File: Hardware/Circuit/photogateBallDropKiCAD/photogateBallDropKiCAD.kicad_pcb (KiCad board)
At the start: 2 copper layers, 127 x 68.6 mm, 56 parts, among them Q1 2N3906, Q2 2N3904, Q3 2N3904, Q4 BPW40, Q5 2N3904, Q6 2N3904, Q7 2N3904, Q8 2N3904, SW2 SW_SPDT, U2 LM358

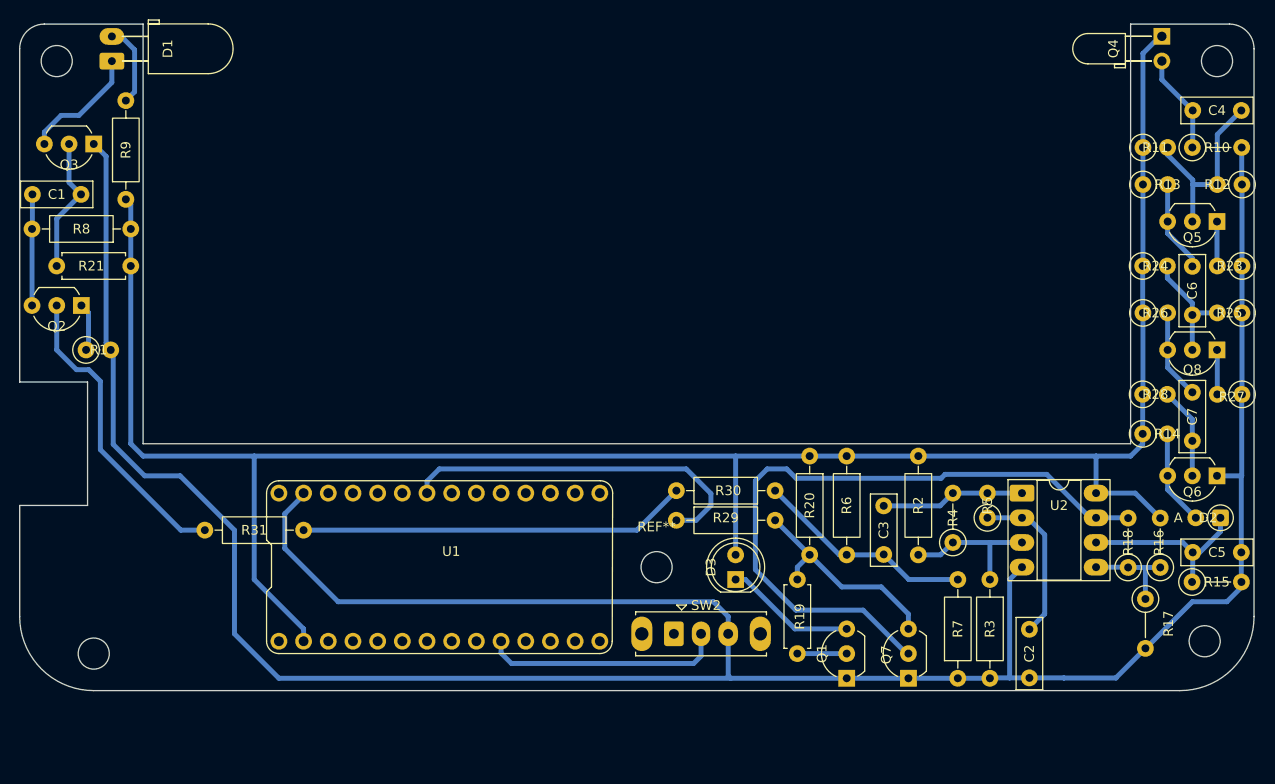
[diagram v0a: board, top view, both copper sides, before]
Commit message: Add photogate PCB
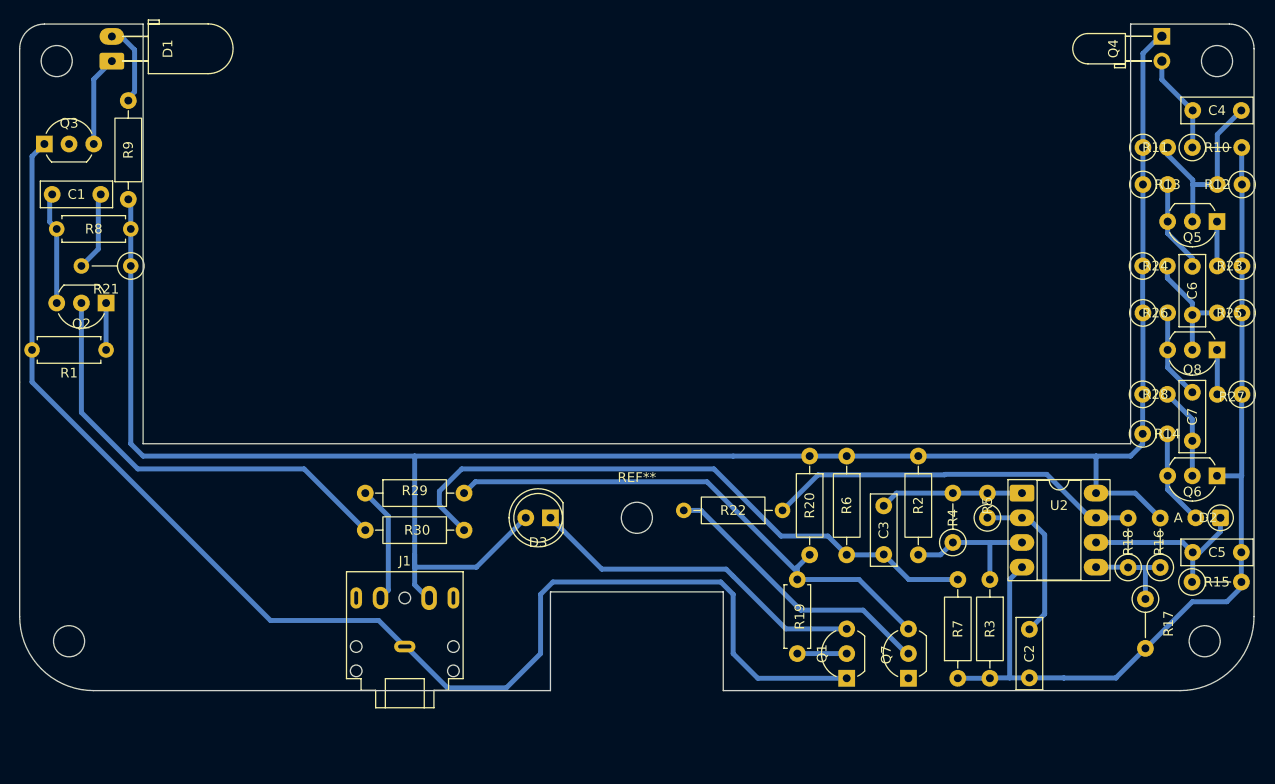
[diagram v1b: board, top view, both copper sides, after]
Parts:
- removed R31: 0, Resistor_THT:R_Axial_DIN0207_L6.3mm_D2.5mm_P10.16mm_Horizontal
- removed SW2: SW_SPDT, User:SlideSwitch_SPDT
- removed U1: ~, User:AdafruitItsyBitsyM0
- added J1: AudioJack3_SwitchTR, Connector_Audio:Jack_3.5mm_CUI_SJ1-3525N_Horizontal, F.Cu at (65.0, 89.4)
- added R22: 0, Resistor_THT:R_Axial_DIN0207_L6.3mm_D2.5mm_P10.16mm_Horizontal, F.Cu at (103.9, 75.4)
- C4: value 4n7 -> 1n
- R1: footprint Resistor_THT:R_Axial_DIN0207_L6.3mm_D2.5mm_P2.54mm_Vertical -> Resistor_THT:R_Axial_DIN0207_L6.3mm_D2.5mm_P7.62mm_Horizontal
- R21: footprint Resistor_THT:R_Axial_DIN0207_L6.3mm_D2.5mm_P7.62mm_Horizontal -> Resistor_THT:R_Axial_DIN0207_L6.3mm_D2.5mm_P5.08mm_Vertical
- R8: footprint Resistor_THT:R_Axial_DIN0207_L6.3mm_D2.5mm_P10.16mm_Horizontal -> Resistor_THT:R_Axial_DIN0207_L6.3mm_D2.5mm_P7.62mm_Horizontal
- moved R30 32.3 mm to (71.1, 77.5)
- moved R29 32.1 mm to (61.0, 73.7)
- moved D3 20.1 mm to (80.0, 76.2), turned to 180 degrees
- moved REF** 5.47 mm to (88.9, 76.2)
- moved Q3 5.08 mm to (27.9, 37.7), turned to 0 degrees
- moved REF** 2.84 mm to (30.5, 88.9)
- moved Q2 2.55 mm to (34.3, 54.1)
- moved R1 2.06 mm to (34.3, 58.9), turned to 180 degrees
- moved C1 2.03 mm to (28.7, 42.9)
- moved R9 0.25 mm to (36.6, 43.4)
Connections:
- R18 pad 2: Net-(Q7-B) -> Net-(R18-Pad2)
- R30 pad 2: Net-(R30-Pad2) -> Net-(Q2-B)
- U2 pad 7: Net-(Q7-B) -> Net-(R18-Pad2)
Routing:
- net GND: track 289.1 -> 230.5 mm
- net Net-(C3-Pad2): track 22.6 -> 64.1 mm
- net Net-(Q7-B): track 69.8 -> 29.2 mm
- net Net-(R30-Pad2): track 40.0 -> 0.00 mm
- net Net-(R18-Pad2): track 0.00 -> 39.0 mm
- net Net-(Q7-C): track 22.3 -> 56.0 mm
- net INT: track 37.4 -> 12.1 mm
- net Net-(SW2-B): track 24.8 -> 0.00 mm
- net Net-(D3-K): track 13.5 -> 35.2 mm
- net Net-(Q2-B): track 31.6 -> 45.5 mm
- net Net-(Q3-B): track 14.6 -> 8.09 mm
- net Net-(D1-K): track 12.5 -> 9.30 mm
- net VCC: track 216.2 -> 214.7 mm
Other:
- outline, holes or cut-outs redrawn

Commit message: edit PCB
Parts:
- J1: footprint Connector_Audio:Jack_3.5mm_CUI_SJ1-3525N_Horizontal -> Connector_Audio:Jack_3.5mm_CUI_SJ1-3523N_Horizontal
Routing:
- net GND: track 230.5 -> 241.9 mm
- net Net-(Q3-B): track 8.09 -> 14.6 mm
- net VCC: track 214.7 -> 212.6 mm
- net INT: track 12.1 -> 13.1 mm
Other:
- outline, holes or cut-outs redrawn
- board text removed: "SPDT Switch"

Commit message: edit photogate pcb
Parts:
- removed C7: 1n, Capacitor_THT:C_Rect_L7.2mm_W2.5mm_P5.00mm_FKS2_FKP2_MKS2_MKP2
- removed Q6: 2N3904, Package_TO_SOT_THT:TO-92_Inline_Wide
- removed R12, R14: 10k, Resistor_THT:R_Axial_DIN0207_L6.3mm_D2.5mm_P2.54mm_Vertical
- removed R21: 100k, Resistor_THT:R_Axial_DIN0207_L6.3mm_D2.5mm_P5.08mm_Vertical
- removed R22, R29, R30: 0, Resistor_THT:R_Axial_DIN0207_L6.3mm_D2.5mm_P10.16mm_Horizontal
- removed R23: 220, Resistor_THT:R_Axial_DIN0207_L6.3mm_D2.5mm_P2.54mm_Vertical
- removed R25: 100k, Resistor_THT:R_Axial_DIN0207_L6.3mm_D2.5mm_P2.54mm_Vertical
- removed R27: 1k, Resistor_THT:R_Axial_DIN0207_L6.3mm_D2.5mm_P2.54mm_Vertical
- removed R28: 1M, Resistor_THT:R_Axial_DIN0207_L6.3mm_D2.5mm_P2.54mm_Vertical
- added C10: 100u, Capacitor_THT:C_Radial_D8.0mm_H7.0mm_P3.50mm, F.Cu at (77.6, 81.0)
- added C11: 1u, Capacitor_THT:C_Rect_L7.2mm_W2.5mm_P5.00mm_FKS2_FKP2_MKS2_MKP2, F.Cu at (120.9, 77.5)
- added C12: 10u, Capacitor_THT:C_Rect_L7.2mm_W2.5mm_P5.00mm_FKS2_FKP2_MKS2_MKP2, F.Cu at (74.5, 91.9)
- added C9: 10u, Capacitor_THT:C_Rect_L7.2mm_W2.5mm_P5.00mm_FKS2_FKP2_MKS2_MKP2, F.Cu at (120.9, 73.8)
- C1: value 1n -> 10n
- C3: value 10n -> 1n
- C5: value 4n7 -> 1n
- D2: footprint Diode_THT:D_DO-35_SOD27_P2.54mm_Vertical_AnodeUp -> Diode_THT:D_DO-35_SOD27_P7.62mm_Horizontal
- J1: value AudioJack3_SwitchTR -> AudioJack3
- R1: value 2k2 -> 1k; footprint Resistor_THT:R_Axial_DIN0207_L6.3mm_D2.5mm_P7.62mm_Horizontal -> Resistor_THT:R_Axial_DIN0207_L6.3mm_D2.5mm_P10.16mm_Horizontal
- R10: value 360 -> 220; footprint Resistor_THT:R_Axial_DIN0207_L6.3mm_D2.5mm_P5.08mm_Vertical -> Resistor_THT:R_Axial_DIN0207_L6.3mm_D2.5mm_P7.62mm_Horizontal
- R11: value 22k -> 100k; footprint Resistor_THT:R_Axial_DIN0207_L6.3mm_D2.5mm_P2.54mm_Vertical -> Resistor_THT:R_Axial_DIN0207_L6.3mm_D2.5mm_P7.62mm_Horizontal
- R13: value 2k2 -> 10k; footprint Resistor_THT:R_Axial_DIN0207_L6.3mm_D2.5mm_P2.54mm_Vertical -> Resistor_THT:R_Axial_DIN0207_L6.3mm_D2.5mm_P7.62mm_Horizontal
- R15, R17, R4: footprint Resistor_THT:R_Axial_DIN0207_L6.3mm_D2.5mm_P5.08mm_Vertical -> Resistor_THT:R_Axial_DIN0207_L6.3mm_D2.5mm_P10.16mm_Horizontal
- R16: value 47k -> 100k; footprint Resistor_THT:R_Axial_DIN0207_L6.3mm_D2.5mm_P5.08mm_Vertical -> Resistor_THT:R_Axial_DIN0207_L6.3mm_D2.5mm_P10.16mm_Horizontal
- R18: value 33k -> 100k; footprint Resistor_THT:R_Axial_DIN0207_L6.3mm_D2.5mm_P5.08mm_Vertical -> Resistor_THT:R_Axial_DIN0207_L6.3mm_D2.5mm_P10.16mm_Horizontal
- R19: value 220 -> 1k; footprint Resistor_THT:R_Axial_DIN0207_L6.3mm_D2.5mm_P7.62mm_Horizontal -> Resistor_THT:R_Axial_DIN0207_L6.3mm_D2.5mm_P10.16mm_Horizontal
- R24: value 220k -> 1M; footprint Resistor_THT:R_Axial_DIN0207_L6.3mm_D2.5mm_P2.54mm_Vertical -> Resistor_THT:R_Axial_DIN0207_L6.3mm_D2.5mm_P7.62mm_Horizontal
- R26: footprint Resistor_THT:R_Axial_DIN0207_L6.3mm_D2.5mm_P2.54mm_Vertical -> Resistor_THT:R_Axial_DIN0207_L6.3mm_D2.5mm_P7.62mm_Horizontal
- R3: footprint Resistor_THT:R_Axial_DIN0207_L6.3mm_D2.5mm_P10.16mm_Horizontal -> Resistor_THT:R_Axial_DIN0207_L6.3mm_D2.5mm_P7.62mm_Horizontal
- R5: value 1k3 -> 1k; footprint Resistor_THT:R_Axial_DIN0207_L6.3mm_D2.5mm_P2.54mm_Vertical -> Resistor_THT:R_Axial_DIN0207_L6.3mm_D2.5mm_P7.62mm_Horizontal
- R6: value 22k -> 1M; footprint Resistor_THT:R_Axial_DIN0207_L6.3mm_D2.5mm_P10.16mm_Horizontal -> Resistor_THT:R_Axial_DIN0207_L6.3mm_D2.5mm_P7.62mm_Horizontal
- R7: value 10k -> 220
- moved R6 75.2 mm to (36.8, 54.7), turned to 180 degrees
- moved Q7 68.3 mm to (48.5, 92.7)
- moved R7 63.4 mm to (59.8, 80.0)
- moved Q1 56.1 mm to (54.4, 92.7)
- moved R19 54.1 mm to (52.3, 71.9)
- moved R20 50.7 mm to (56.0, 69.8)
- moved C3 37.3 mm to (77.0, 74.5), turned to 180 degrees
- moved C2 25.6 mm to (104.4, 81.8)
- moved R4 21.3 mm to (100.8, 84.3)
- moved R2 20.8 mm to (97.0, 69.8)
- moved R1 18.9 mm to (48.0, 71.9), turned to -90 degrees
- moved R5 17.8 mm to (108.1, 81.8)
- moved R3 17.3 mm to (108.1, 84.7)
- moved U2 17.0 mm to (113.3, 81.2)
- moved R18 15.5 mm to (124.8, 86.6)
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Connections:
- C1 pad 1: Net-(Q2-C) -> GND
- C1 pad 2: Net-(Q3-B) -> VCC
- C3 pad 2: Net-(C3-Pad2) -> Net-(Q2-B)
- D3 pad 2: VCC -> Net-(D3-A)
- Q2 pad 1: Net-(Q2-E) -> GND
- Q3 pad 2: Net-(Q3-B) -> Net-(Q2-C)
- Q5 pad 1: Net-(Q5-E) -> GND
- Q7 pad 3: Net-(Q7-C) -> INT
- Q8 pad 1: Net-(Q8-E) -> GND
- Q8 pad 3: Net-(Q8-C) -> Net-(D2-A)
- R1 pad 1: Net-(Q2-E) -> Net-(R1-Pad1)
- R1 pad 2: GND -> Net-(Q7-B)
- R18 pad 2: Net-(R18-Pad2) -> Net-(R1-Pad1)
- R19 pad 1: Net-(Q7-C) -> Net-(R1-Pad1)
- R20 pad 2: Net-(Q7-C) -> INT
- R26 pad 2: Net-(Q8-C) -> Net-(D2-A)
- R6 pad 2: Net-(C3-Pad2) -> Net-(Q2-B)
- R7 pad 1: GND -> Net-(D3-A)
- R7 pad 2: Net-(C3-Pad2) -> VCC
- U2 pad 7: Net-(R18-Pad2) -> Net-(R1-Pad1)
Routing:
- net Net-(R1-Pad1): track 0.00 -> 91.5 mm, vias 0 -> 2
- net Net-(C3-Pad2): track 64.1 -> 0.00 mm
- net Net-(Q7-C): track 56.0 -> 0.00 mm
- net Net-(R18-Pad2): track 39.0 -> 0.00 mm
- net Net-(C3-Pad1): track 14.8 -> 46.7 mm
- net Net-(D2-K): track 18.6 -> 41.3 mm
- net GND: track 241.9 -> 261.6 mm
- net Net-(D3-K): track 35.2 -> 16.4 mm
- net Net-(Q7-B): track 29.2 -> 10.7 mm
- net Net-(Q3-B): track 14.6 -> 0.00 mm
- net Net-(Q2-B): track 45.5 -> 60.0 mm
- net Net-(Q5-B): track 19.9 -> 7.17 mm
- net Net-(Q6-B): track 9.45 -> 0.00 mm
- net Net-(Q8-C): track 9.22 -> 0.00 mm
- net Net-(U2A--): track 17.0 -> 9.68 mm
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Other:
- outline, holes or cut-outs redrawn

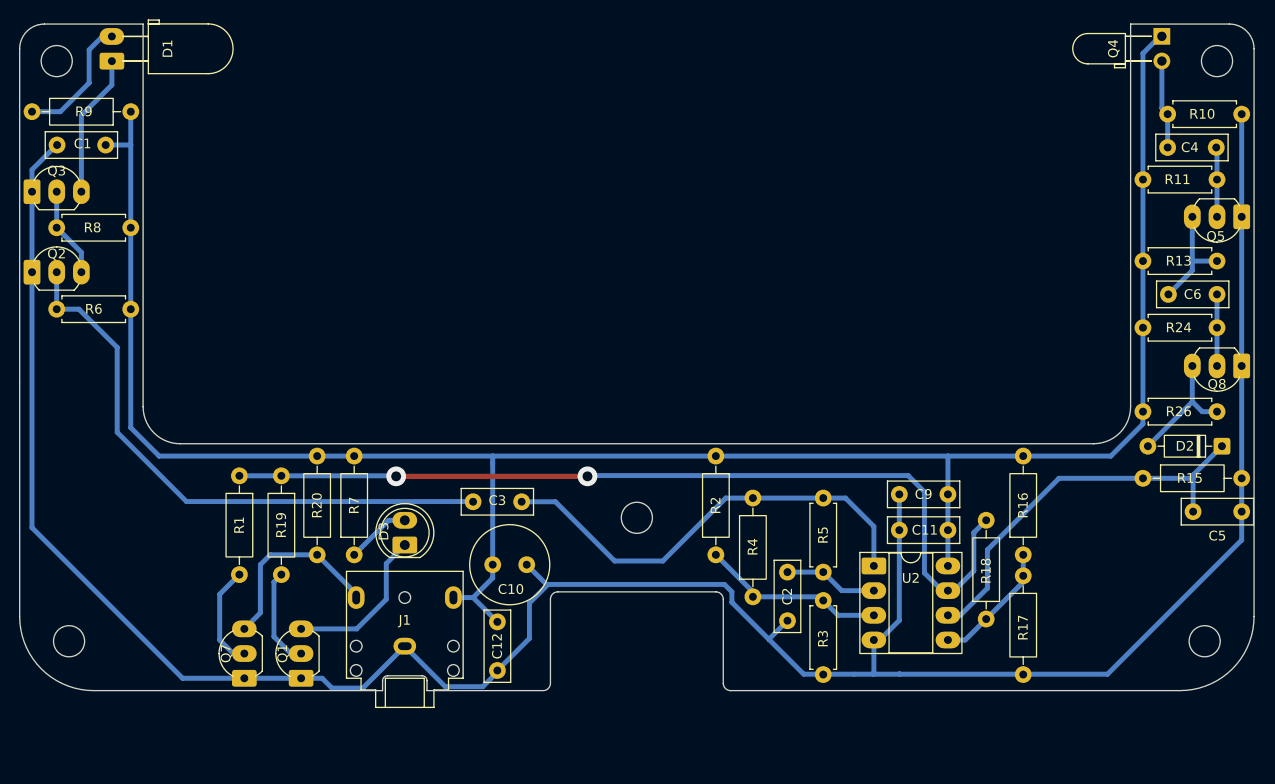
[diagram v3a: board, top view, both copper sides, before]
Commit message: Edit attachment point
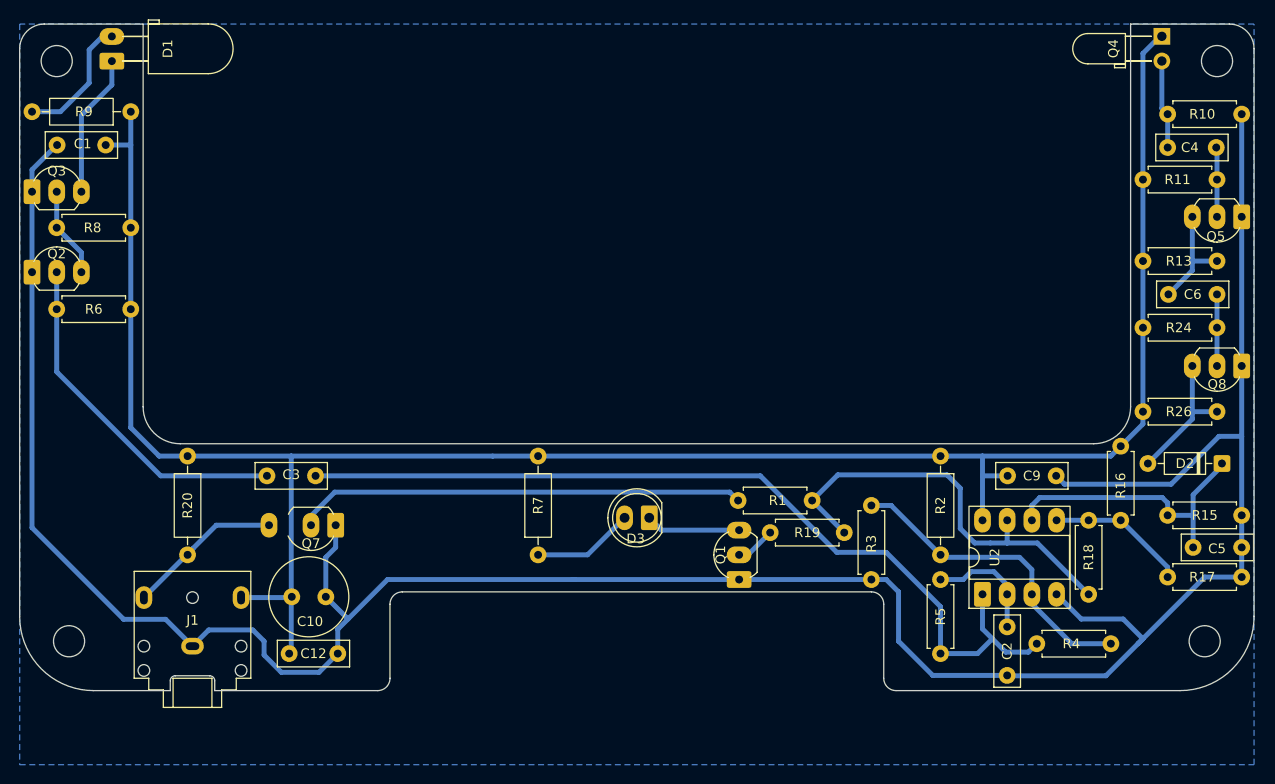
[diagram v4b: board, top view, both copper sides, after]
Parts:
- removed C11: 1u, Capacitor_THT:C_Rect_L7.2mm_W2.5mm_P5.00mm_FKS2_FKP2_MKS2_MKP2
- removed the REF** at (88.9, 76.2)
- R1, R15, R16, R17, R18, R19, R4: footprint Resistor_THT:R_Axial_DIN0207_L6.3mm_D2.5mm_P10.16mm_Horizontal -> Resistor_THT:R_Axial_DIN0207_L6.3mm_D2.5mm_P7.62mm_Horizontal
- moved R1 59.0 mm to (106.9, 74.4), turned to 180 degrees
- moved R19 58.2 mm to (110.2, 77.7), turned to 180 degrees
- moved Q1 46.2 mm to (99.4, 82.5)
- moved R4 37.1 mm to (137.7, 89.2), turned to 180 degrees
- moved D3 25.3 mm to (90.2, 76.2), turned to 180 degrees
- moved C2 23.3 mm to (127.0, 87.4)
- moved R2 23.1 mm to (120.1, 69.8)
- moved J1 21.8 mm to (43.2, 89.4)
- moved C3 21.4 mm to (55.8, 71.9)
- moved C10 20.9 mm to (56.9, 84.3)
- moved R7 18.9 mm to (78.7, 80.0)
- moved Q7 18.3 mm to (57.9, 77.0), turned to 180 degrees
- moved C12 16.5 mm to (58.1, 90.2), turned to 180 degrees
- moved R17 14.9 mm to (143.5, 82.3), turned to 0 degrees
- moved R18 14.6 mm to (135.4, 76.5), turned to -90 degrees
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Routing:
- net Net-(R1-Pad1): track 91.5 -> 45.6 mm, vias 2 -> 0
- net Net-(C3-Pad1): track 46.7 -> 91.2 mm
- net Net-(Q7-B): track 10.7 -> 46.3 mm
- net Net-(Q2-B): track 60.0 -> 36.3 mm
- net GND: track 261.6 -> 282.0 mm
- net Net-(U2A-+): track 19.1 -> 32.6 mm
- net Net-(D2-K): track 41.3 -> 30.4 mm
- net Net-(D3-K): track 16.4 -> 9.77 mm
- net Net-(Q1-B): track 10.2 -> 4.14 mm
- net Net-(D3-A): track 6.68 -> 10.5 mm
- net INT: track 19.6 -> 16.0 mm
- net VCC: track 214.9 -> 217.4 mm
- net Net-(U2A--): track 9.68 -> 12.1 mm
- net Net-(U2B-+): track 13.0 -> 14.7 mm
- net Net-(D2-A): track 13.1 -> 14.5 mm
- added copper zone on B.Cu, net GND
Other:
- outline, holes or cut-outs redrawn
